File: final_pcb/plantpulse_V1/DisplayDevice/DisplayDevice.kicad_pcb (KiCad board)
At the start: 2 copper layers, 119 x 64.2 mm, 10 parts, among them J1 SSD1306, M1 X27.168

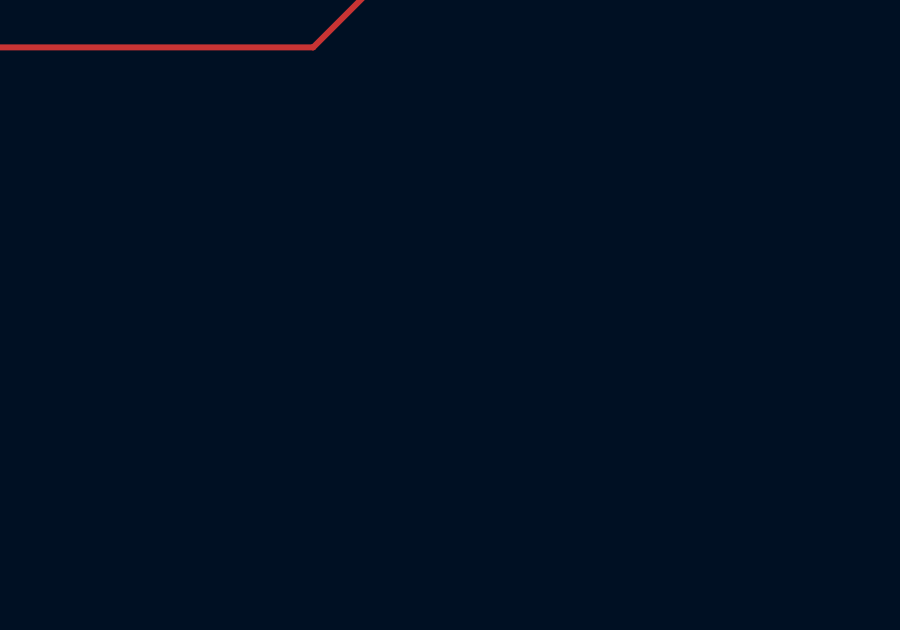
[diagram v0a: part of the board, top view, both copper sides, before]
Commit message: src code for sensing device update
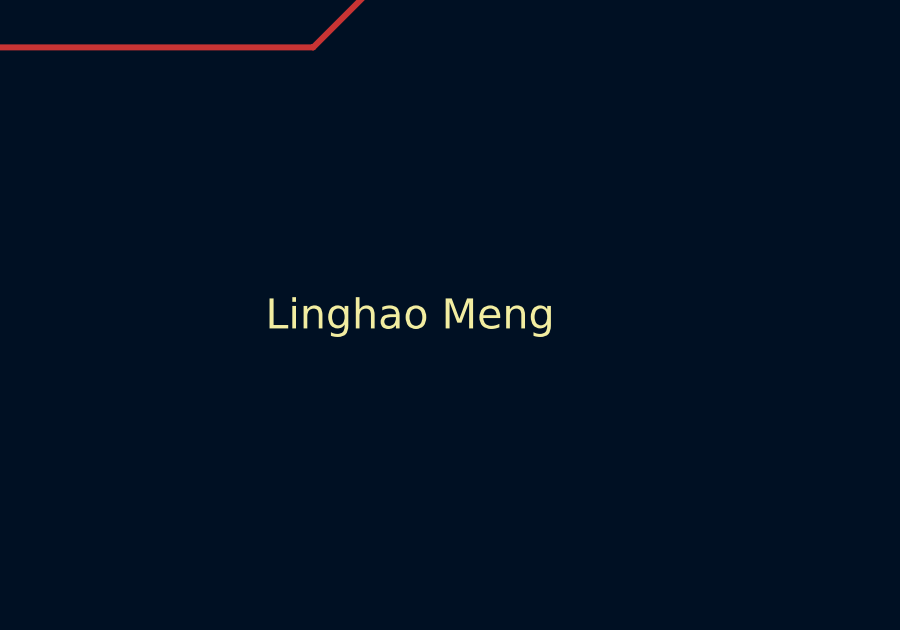
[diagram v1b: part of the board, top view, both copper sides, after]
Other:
- board text added: "Linghao Meng"
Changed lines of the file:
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@@
 		(layer "Edge.Cuts")
+	)
+	(gr_text "Linghao Meng"
+		(at 125.5 117.0515 0)
+		(layer "F.SilkS")
+		(effects
+			(font
+				(size 1 1)
+				(thickness 0.1)
+			)
+			(justify left bottom)
+		)
 	)
 	(segment
